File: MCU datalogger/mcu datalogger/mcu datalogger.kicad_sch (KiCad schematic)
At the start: 0 parts

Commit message: Added values to the components.
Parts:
- added BT1: Battery, symbol Device:Battery
- added C1, C4: 0.1uF, symbol Device:C
- added C2, C3: 22pF, symbol Device:C
- added C5: 100nF, symbol Device:C_Polarized
- added D1, D2: LED, symbol Device:LED
- added H1, H2, H3, H4: MountingHole, symbol Mechanical:MountingHole
- added R1, R2: 4.7K, symbol Device:R
- added R3, R4, R6: 10K, symbol Device:R
- added R5, R7: 330, symbol Device:R
- added U1, U3: 24LC1025, symbol Memory_EEPROM:24LC1025
- added U2: DS1337S_, DS1337S_:SOIC127P600X175-8N, symbol DS1337S_:DS1337S_
- added U4: ATMEGA328P-AU, ATMEGA328P-AU:QFP80P900X900X120-32N, symbol ATMEGA328P-AU:ATMEGA328P-AU
- added Y1: 32.768 KHz, symbol Device:Crystal
- added Y2: 16MHz, symbol Device:Crystal
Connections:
- new net: U4.21 (GND), U4.3 (GND), U4.5 (GND)
- new net: U4.4 (VCC), U4.6 (VCC)
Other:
- added sheet Connectors (Connectors.kicad_sch)

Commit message: Completed the footprints association.
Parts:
- BT1: footprint (none) -> Connector_PinHeader_2.54mm:PinHeader_1x02_P2.54mm_Vertical
- C1, C2, C3, C4, C5: footprint (none) -> Capacitor_SMD:C_0805_2012Metric
- D1, D2: footprint (none) -> LED_SMD:LED_0805_2012Metric
- H1, H2, H3, H4: footprint (none) -> MountingHole:MountingHole_2.1mm
- R1, R2, R3, R4, R5, R6, R7: footprint (none) -> Resistor_SMD:R_0805_2012Metric
- U1, U3: footprint (none) -> Package_SO:SOIC-8_3.9x4.9mm_P1.27mm
- U2: footprint DS1337S_:SOIC127P600X175-8N -> Footprints:SOIC127P600X175-8N
- U4: footprint ATMEGA328P-AU:QFP80P900X900X120-32N -> Footprints:QFP80P900X900X120-32N
- Y1, Y2: footprint (none) -> Crystal:Crystal_SMD_5032-2Pin_5.0x3.2mm_HandSoldering
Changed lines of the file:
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@@
       (effects (font (size 1.27 1.27)) (justify left))
     )
-    (property "Footprint" "" (at 194.31 132.08 0)
+    (property "Footprint" "MountingHole:MountingHole_2.1mm" (at 194.31 132.08 0)
       (effects (font (size 1.27 1.27)) hide)
     )
@@
       (effects (font (size 1.27 1.27)))
     )
-    (property "Footprint" "DS1337S_:SOIC127P600X175-8N" (at 69.85 63.5 0)
+    (property "Footprint" "Footprints:SOIC127P600X175-8N" (at 69.85 63.5 0)
       (effects (font (size 1.27 1.27)) (justify bottom) hide)
     )
@@
       (effects (font (size 1.27 1.27)) (justify left))
     )
-    (property "Footprint" "" (at 255.27 50.546 90)
+    (property "Footprint" "Connector_PinHeader_2.54mm:PinHeader_1x02_P2.54mm_Vertical" (at 255.27 50.546 90)
       (effects (font (size 1.27 1.27)) hide)
     )
@@
       (effects (font (size 1.27 1.27)) (justify left))
     )
-    (property "Footprint" "" (at 194.31 123.19 0)
+    (property "Footprint" "MountingHole:MountingHole_2.1mm" (at 194.31 123.19 0)
       (effects (font (size 1.27 1.27)) hide)
     )
@@
       (effects (font (size 1.27 1.27)) (justify left))
     )
-    (property "Footprint" "" (at 151.4348 67.31 0)
+    (property "Footprint" "Capacitor_SMD:C_0805_2012Metric" (at 151.4348 67.31 0)
       (effects (font (size 1.27 1.27)) hide)
     )
@@
       (effects (font (size 1.27 1.27)) (justify left))
     )
-    (property "Footprint" "" (at 52.832 119.38 90)
+    (property "Footprint" "Resistor_SMD:R_0805_2012Metric" (at 52.832 119.38 90)
       (effects (font (size 1.27 1.27)) hide)
     )
@@
       (effects (font (size 1.27 1.27)))
     )
-    (property "Footprint" "" (at 237.49 52.3748 0)
+    (property "Footprint" "Capacitor_SMD:C_0805_2012Metric" (at 237.49 52.3748 0)
       (effects (font (size 1.27 1.27)) hide)
     )
@@
       (effects (font (size 1.27 1.27)) (justify left))
     )
-    (property "Footprint" "" (at 238.252 81.28 90)
+    (property "Footprint" "Resistor_SMD:R_0805_2012Metric" (at 238.252 81.28 90)
       (effects (font (size 1.27 1.27)) hide)
     )
@@
       (effects (font (size 1.27 1.27)) (justify left))
     )
-    (property "Footprint" "" (at 102.362 53.34 90)
+    (property "Footprint" "Resistor_SMD:R_0805_2012Metric" (at 102.362 53.34 90)
       (effects (font (size 1.27 1.27)) hide)
     )
@@
       (effects (font (size 1.27 1.27)))
     )
-    (property "Footprint" "" (at 34.29 58.42 0)
+    (property "Footprint" "Crystal:Crystal_SMD_5032-2Pin_5.0x3.2mm_HandSoldering" (at 34.29 58.42 0)
       (effects (font (size 1.27 1.27)) hide)
     )
@@
       (effects (font (size 1.27 1.27)) (justify left))
     )
-    (property "Footprint" "" (at 154.178 50.8 90)
+    (property "Footprint" "Resistor_SMD:R_0805_2012Metric" (at 154.178 50.8 90)
       (effects (font (size 1.27 1.27)) hide)
     )
@@
       (effects (font (size 1.27 1.27)) (justify left))
     )
-    (property "Footprint" "" (at 43.18 138.43 0)
+    (property "Footprint" "Package_SO:SOIC-8_3.9x4.9mm_P1.27mm" (at 43.18 138.43 0)
       (effects (font (size 1.27 1.27)) hide)
     )
@@
       (effects (font (size 1.27 1.27)) (justify left))
     )
-    (property "Footprint" "" (at 93.472 53.34 90)
+    (property "Footprint" "Resistor_SMD:R_0805_2012Metric" (at 93.472 53.34 90)
       (effects (font (size 1.27 1.27)) hide)
     )
@@
       (effects (font (size 1.27 1.27)) (justify right))
     )
-    (property "Footprint" "" (at 240.03 66.04 0)
+    (property "Footprint" "LED_SMD:LED_0805_2012Metric" (at 240.03 66.04 0)
       (effects (font (size 1.27 1.27)) hide)
     )
@@
       (effects (font (size 1.27 1.27)) (justify left))
     )
-    (property "Footprint" "" (at 65.532 119.38 90)
+    (property "Footprint" "Resistor_SMD:R_0805_2012Metric" (at 65.532 119.38 90)
       (effects (font (size 1.27 1.27)) hide)
     )
@@
       (effects (font (size 1.27 1.27)) (justify left))
     )
-    (property "Footprint" "" (at 78.74 138.43 0)
+    (property "Footprint" "Package_SO:SOIC-8_3.9x4.9mm_P1.27mm" (at 78.74 138.43 0)
       (effects (font (size 1.27 1.27)) hide)
     )
@@
       (effects (font (size 1.27 1.27)) (justify left))
     )
-    (property "Footprint" "" (at 194.31 140.97 0)
+    (property "Footprint" "MountingHole:MountingHole_2.1mm" (at 194.31 140.97 0)
       (effects (font (size 1.27 1.27)) hide)
     )
@@
       (effects (font (size 1.27 1.27)) (justify right))
     )
-    (property "Footprint" "" (at 153.3652 78.74 0)
+    (property "Footprint" "Capacitor_SMD:C_0805_2012Metric" (at 153.3652 78.74 0)
       (effects (font (size 1.27 1.27)) hide)
     )
@@
       (effects (font (size 1.27 1.27)) (justify right))
     )
-    (property "Footprint" "" (at 166.37 76.2 0)
+    (property "Footprint" "Crystal:Crystal_SMD_5032-2Pin_5.0x3.2mm_HandSoldering" (at 166.37 76.2 0)
       (effects (font (size 1.27 1.27)) hide)
     )
@@
       (effects (font (size 1.27 1.27)))
     )
-    (property "Footprint" "ATMEGA328P-AU:QFP80P900X900X120-32N" (at 205.74 66.04 0)
+    (property "Footprint" "Footprints:QFP80P900X900X120-32N" (at 205.74 66.04 0)
       (effects (font (size 1.27 1.27)) (justify bottom) hide)
     )
@@
       (effects (font (size 1.27 1.27)) (justify left))
     )
-    (property "Footprint" "" (at 194.31 149.86 0)
+    (property "Footprint" "MountingHole:MountingHole_2.1mm" (at 194.31 149.86 0)
       (effects (font (size 1.27 1.27)) hide)
     )
@@
       (effects (font (size 1.27 1.27)) (justify left))
     )
-    (property "Footprint" "" (at 167.3352 53.34 0)
+    (property "Footprint" "Capacitor_SMD:C_0805_2012Metric" (at 167.3352 53.34 0)
       (effects (font (size 1.27 1.27)) hide)
     )
@@
       (effects (font (size 1.27 1.27)) (justify right))
     )
-    (property "Footprint" "" (at 166.37 62.23 0)
+    (property "Footprint" "LED_SMD:LED_0805_2012Metric" (at 166.37 62.23 0)
       (effects (font (size 1.27 1.27)) hide)
     )
@@
       (effects (font (size 1.27 1.27)) (justify right))
     )
-    (property "Footprint" "" (at 113.3348 57.15 0)
+    (property "Footprint" "Capacitor_SMD:C_0805_2012Metric" (at 113.3348 57.15 0)
       (effects (font (size 1.27 1.27)) hide)
     )
@@
       (effects (font (size 1.27 1.27)))
     )
-    (property "Footprint" "" (at 166.37 88.138 90)
-      (effects (font (size 1.27 1.27)) hide)
-    )
+    (property "Footprint" "Resistor_SMD:R_0805_2012Metric" (at 166.37 88.138 90)
+      (effects (font (size 1.27 1.27)) hide)
+    )

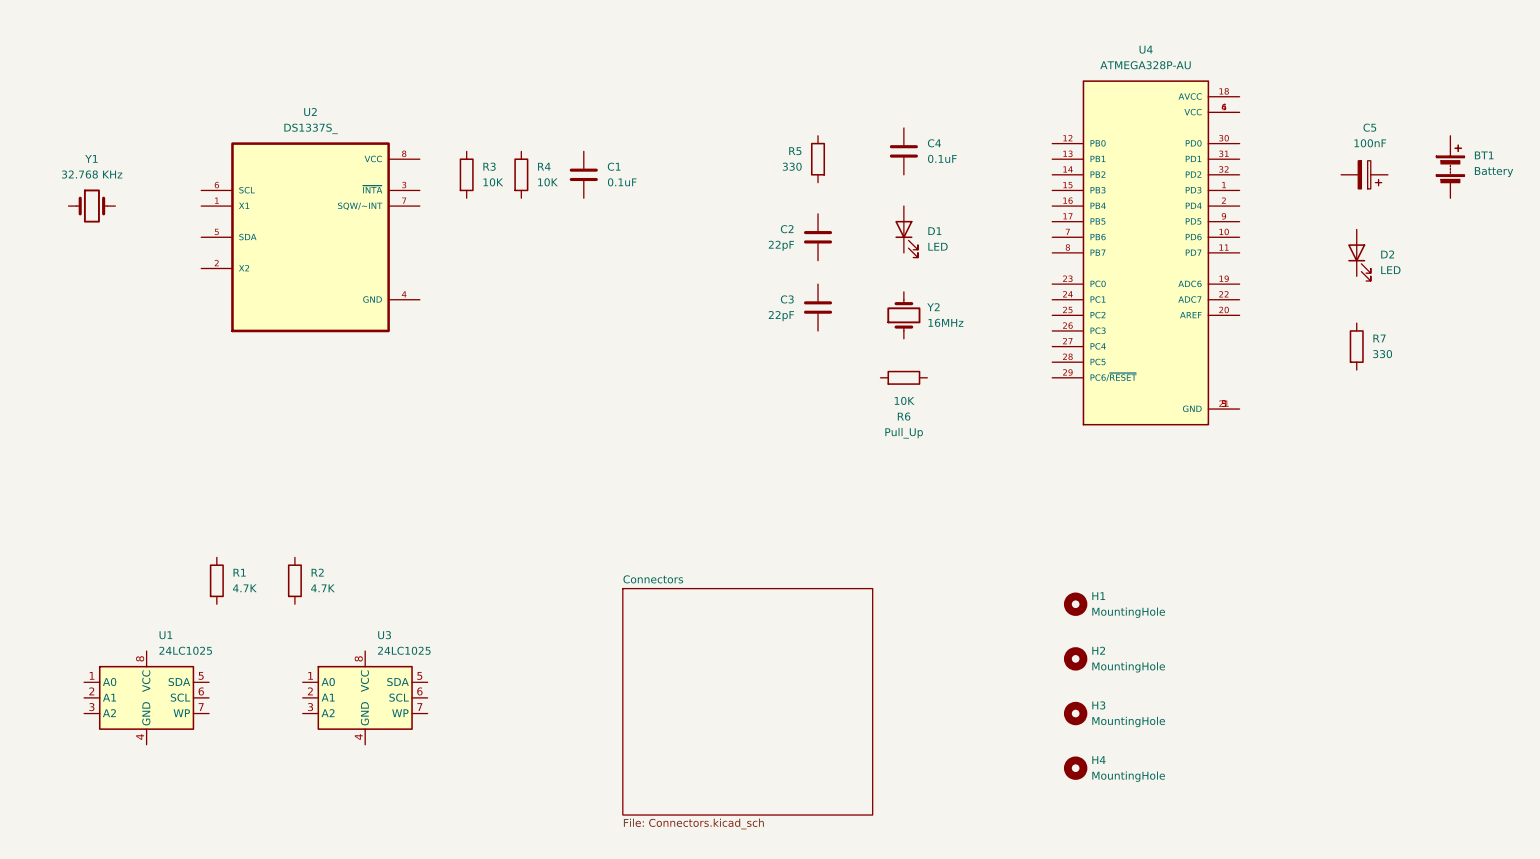
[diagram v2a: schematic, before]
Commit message: Completed the wiring & labeling of the main sheet
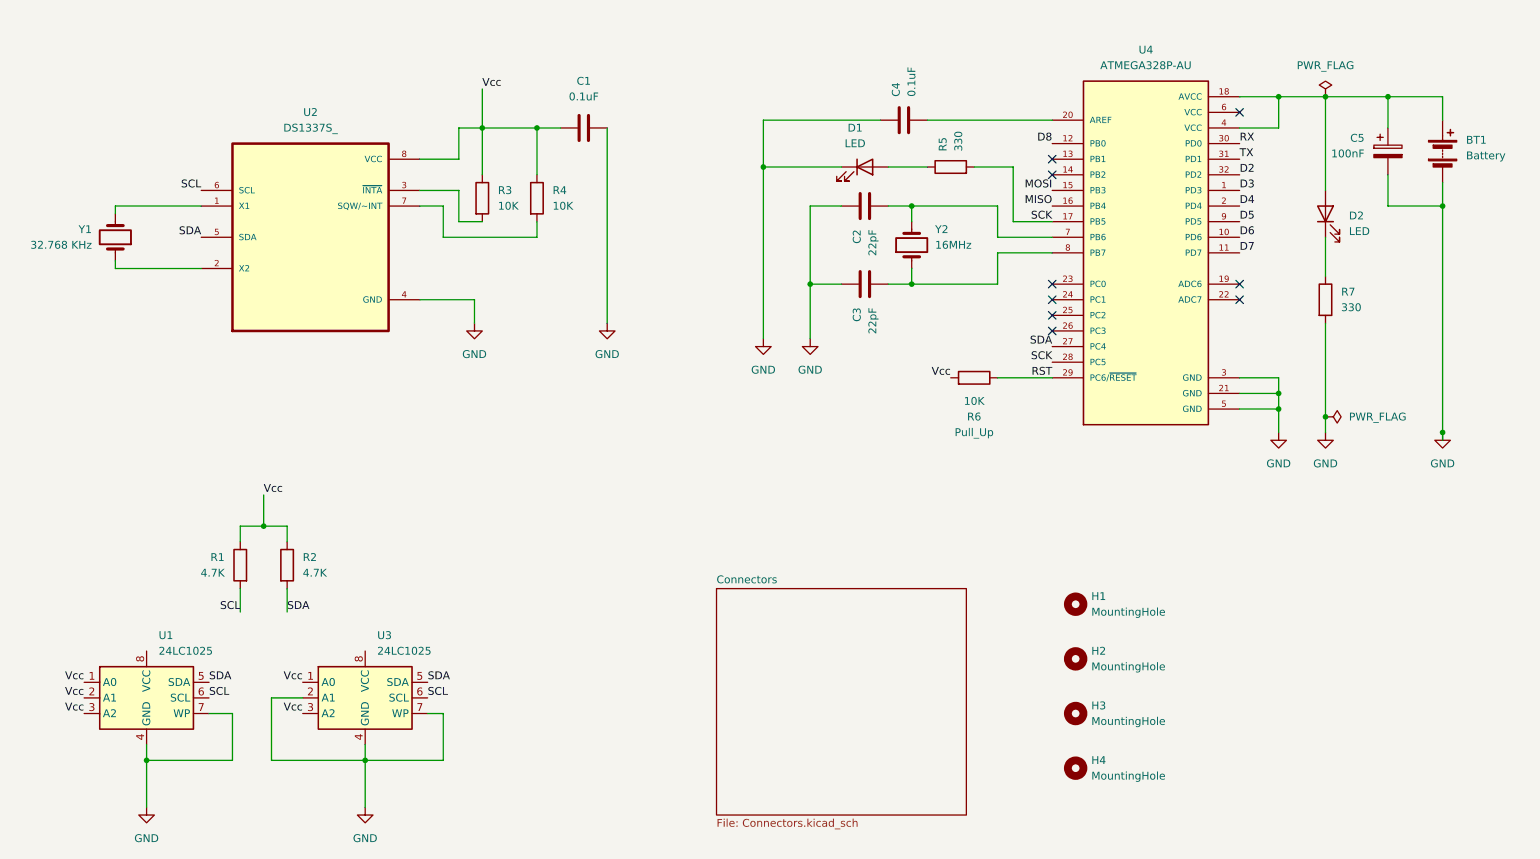
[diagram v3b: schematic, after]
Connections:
- net at U2.1 (X1): now also Y1.2
- net at U2.2 (X2): now also Y1.1
- net at U2.3 (~{INTA}): now also R3.2
- net GND: now reaches U2.4 (GND)
- net GND: now also BT1.2 (-), C1.2, C2.1, C3.1, C4.1, C5.2, D1.1 (K), R7.2, U1.4 (GND), U1.7 (WP), U3.2 (A1), U3.4 (GND), U3.7 (WP), U4.21 (GND), U4.3 (GND), U4.5 (GND)
- net SDA: now reaches U2.5 (SDA)
- net SDA: now also R2.2, U1.5 (SDA), U3.5 (SDA), U4.27 (PC4)
- net SCL: now reaches U2.6 (SCL)
- net SCL: now also R1.2, U1.6 (SCL), U3.6 (SCL)
- net at U2.7 (SQW/~INT): now also R4.2
- net Vcc: now reaches U2.8 (VCC)
- net Vcc: now also C1.1, R1.1, R2.1, R3.1, R4.1, R6.2, U1.1 (A0), U1.2 (A1), U1.3 (A2), U3.1 (A0), U3.3 (A2)
- net at BT1.1 (+): now also C5.1, D2.2 (A), U4.18 (AVCC), U4.4 (VCC)
- net at C2.2: now also U4.7 (PB6), Y2.2
- net at R7.1: now also D2.1 (K)
- net at R5.1: now also D1.2 (A)
- net SCK: now reaches R5.2
- net SCK: now also U4.17 (PB5), U4.28 (PC5)
- net at C3.2: now also U4.8 (PB7), Y2.1
- net D3: now reaches U4.1 (PD3)
- net D6: now reaches U4.10 (PD6)
- net D7: now reaches U4.11 (PD7)
- net D8: now reaches U4.12 (PB0)
- net MOSI: now reaches U4.15 (PB3)
- net MISO: now reaches U4.16 (PB4)
- net D4: now reaches U4.2 (PD4)
- net at U4.20 (AREF): now also C4.2
- net RST: now reaches U4.29 (PC6/~{RESET})
- net RST: now also R6.1
- net RX: now reaches U4.30 (PD0)
- net TX: now reaches U4.31 (PD1)
- net D2: now reaches U4.32 (PD2)
- net at U4.6 (VCC): no longer U4.4 (VCC)
- net D5: now reaches U4.9 (PD5)
- no-connect marks 0 -> 9
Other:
- moved on the sheet: BT1, C1, C2, C3, C4, C5, D1, D2, R1, R2, R3, R4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

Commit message: Completed wiring in the second sheet.
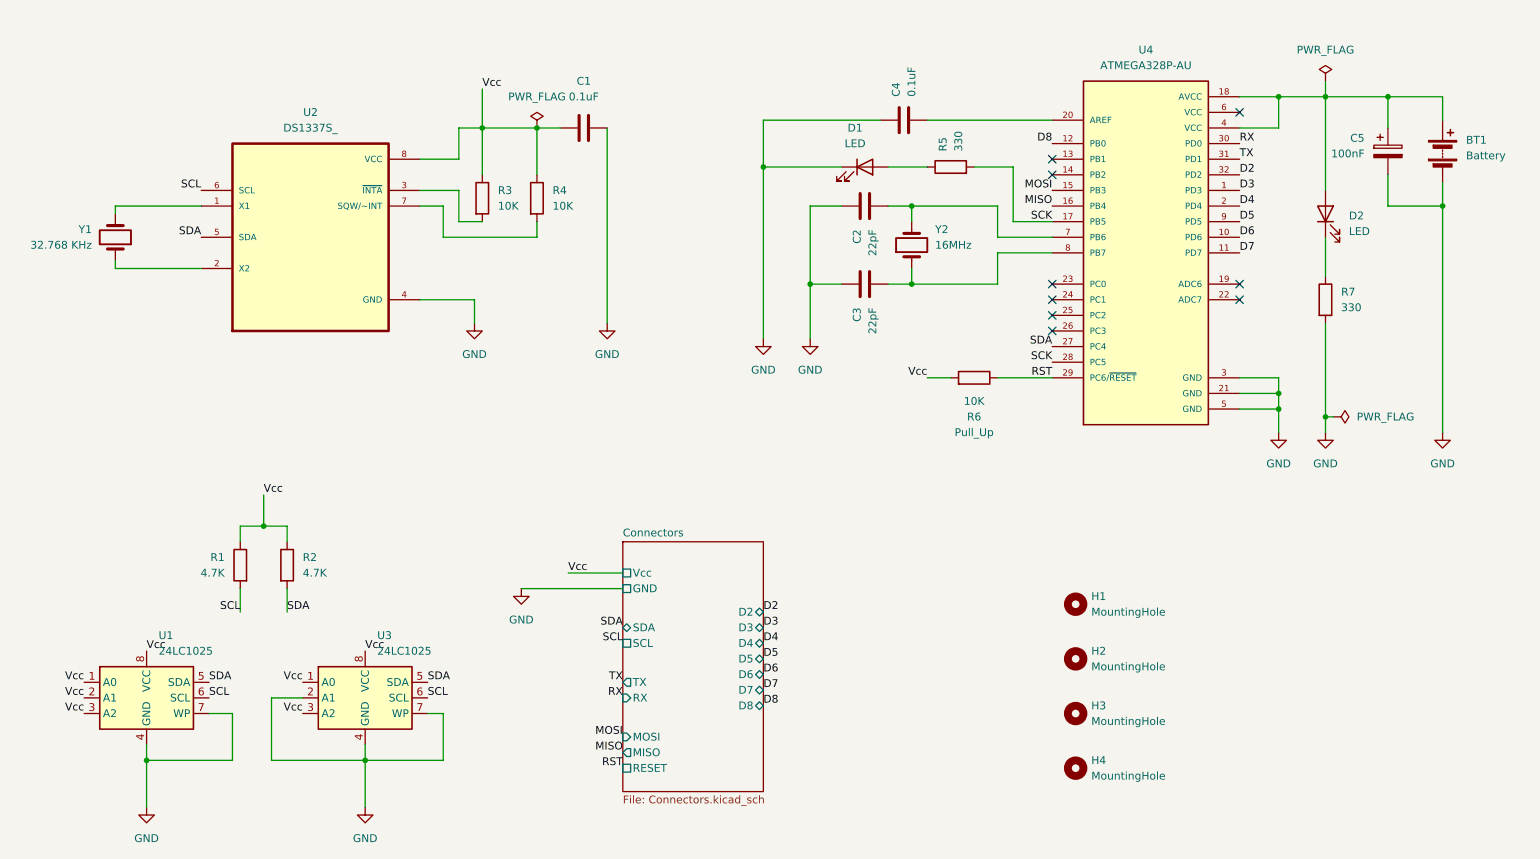
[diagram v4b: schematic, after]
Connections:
- net Vcc: now also U1.8 (VCC), U3.8 (VCC)
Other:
- sheet Connectors ports: added D2, D3, D4, D5, D6, D7, D8, GND, MISO, MOSI, RESET, RX, SCL, SDA, TX, Vcc; removed none

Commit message: Completed the footprints placement.
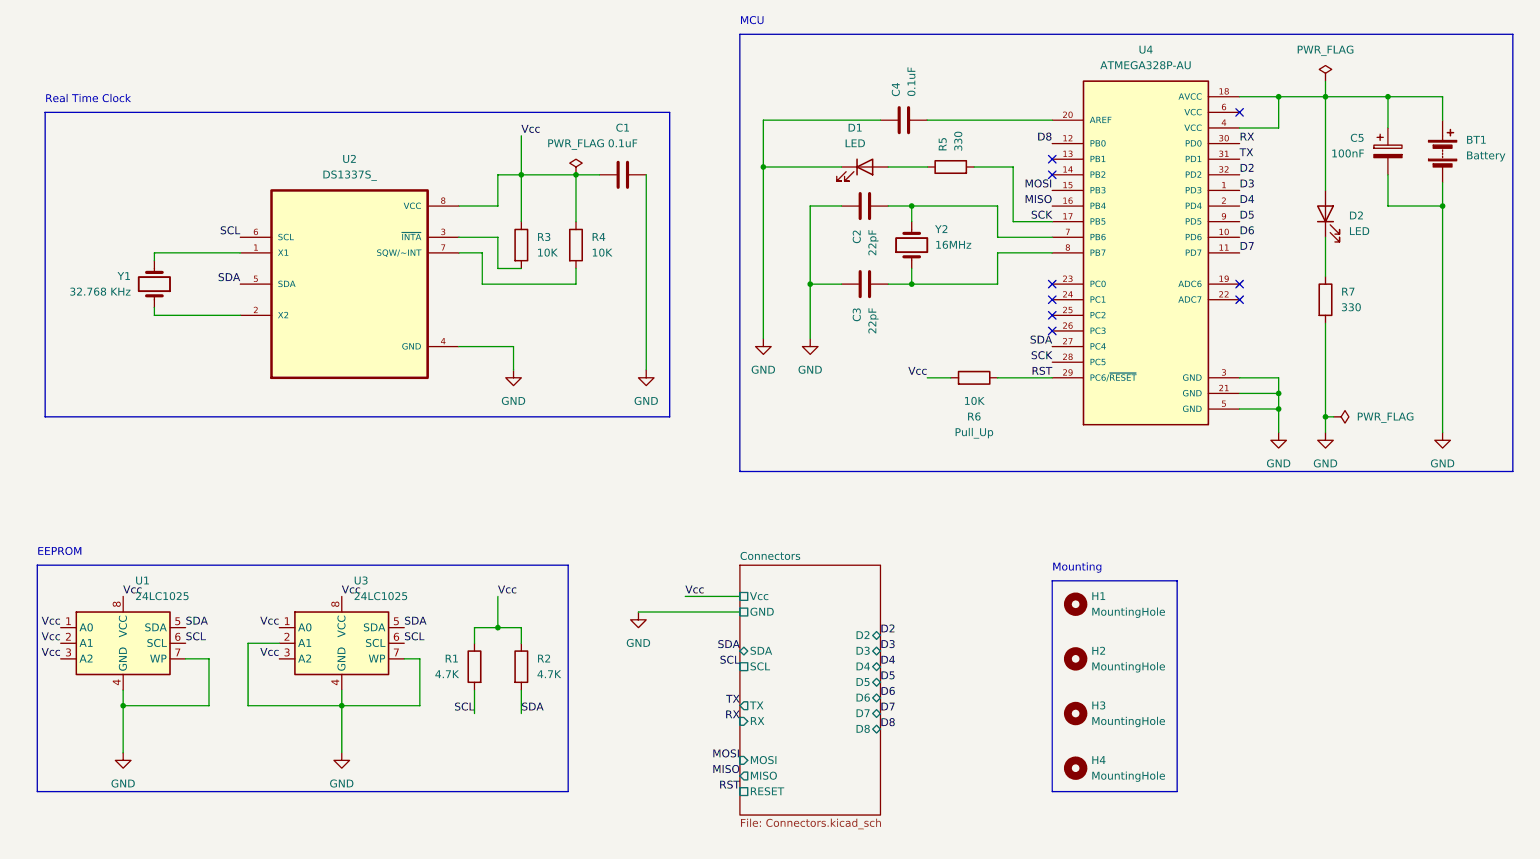
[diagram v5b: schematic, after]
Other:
- note added: "EEPROM"
- note added: "MCU"
- note added: "Mounting"
- note added: "Real Time Clock"
- moved on the sheet: C1, R1, R2, R3, R4, U1, U2, U3, Y1
